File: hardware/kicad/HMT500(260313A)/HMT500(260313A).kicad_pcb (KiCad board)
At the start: 6 copper layers, 56.5 x 23 mm, 110 parts, among them J1 SM08B-GHS-TB, J2 TC2030-IDC-NL, J3 SM04B-SRSS-TB, J5 CHASSIS wire, U1 TPS26600PWPR, U10 TPS26611DDFR, U11 THVD2410DGKR, U12 OPA197IDBVR, U13 OPA197IDBVR, U14 SN74LVC2G32DCUR, U15 LMR51606YFDBVR, U2 LMR51606YFDBVR, U3 TPS7A2033PDBVR, U4 STM32G0B1CCT6, U5 PCAP04-AQFM-24, U6 ADS1220IPWR, U7 DAC8760IPWP, U8 DAC8760IPWP, U9 TPS26611DDFR

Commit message: HMT500 A5 배선 연결 완료 및 제조 검토 패키지 생성
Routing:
- net SWCLK: track 7.07 -> 41.5 mm, vias 0 -> 4
- net RS485_A_EXT: track 2.83 -> 30.3 mm, vias 0 -> 4
- net VIN_P: track 49.8 -> 69.3 mm, vias 6 -> 8
- net OUT1_SGOOD: track 0.82 -> 19.3 mm, vias 0 -> 2
- net DAC_MOSI: track 55.5 -> 44.6 mm, vias 6 -> 5
- net EF_RTN: track 60.4 -> 50.3 mm, vias 8 -> 6
- net VAO: track 95.8 -> 91.0 mm
- net DAC2_LATCH: track 44.5 -> 48.3 mm, vias 5 -> 6
- net +3V3: track 166.7 -> 163.9 mm
- net CDC_SCK: track 17.2 -> 14.5 mm
- net CDC_MOSI: track 9.56 -> 6.89 mm
- net VIN_SENSE: track 13.3 -> 11.0 mm
- net PT_P: track 15.0 -> 13.6 mm
- net SWDIO: track 43.0 -> 41.9 mm
- net DAC2_SCLK: track 34.7 -> 33.7 mm
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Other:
- board text added: "HMT500 A5"
- board text removed: "HMT500 A4"

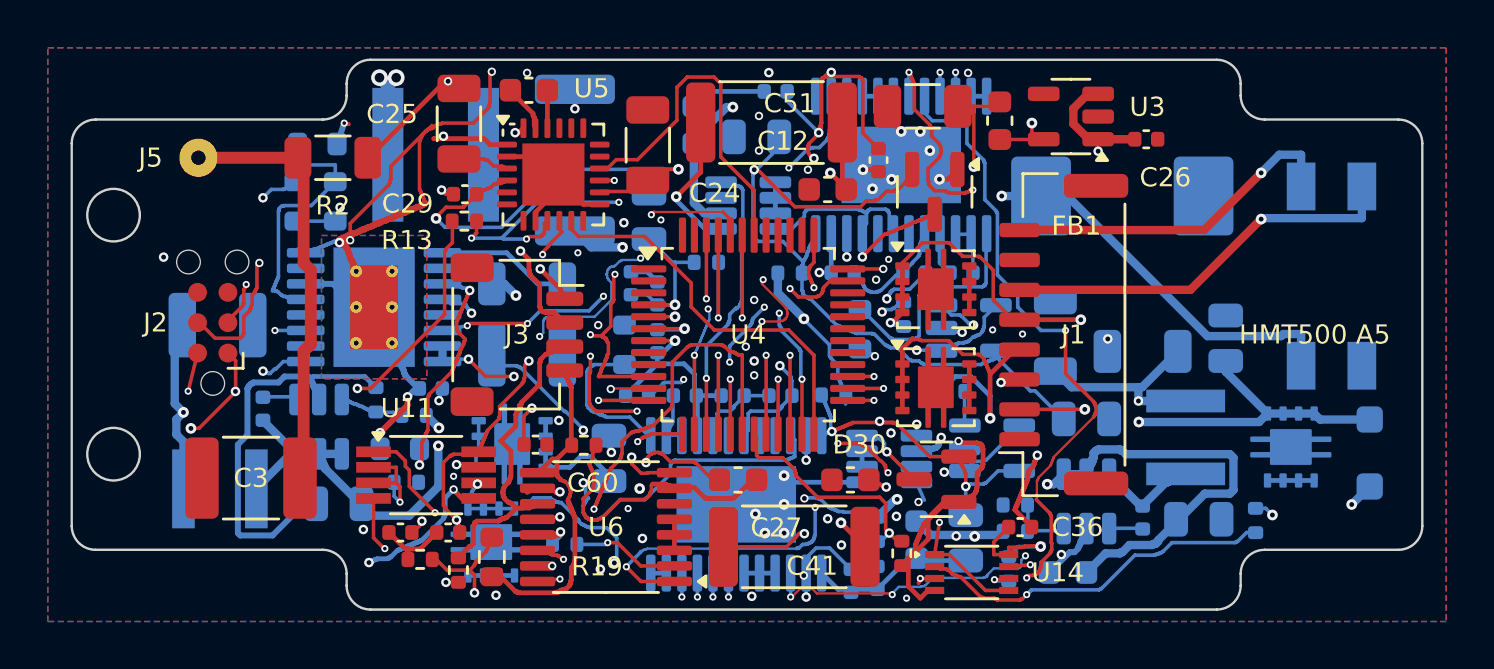
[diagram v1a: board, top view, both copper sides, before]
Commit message: HMT500 A5-R1 실제 실크 근접 배치 및 거버 재생성
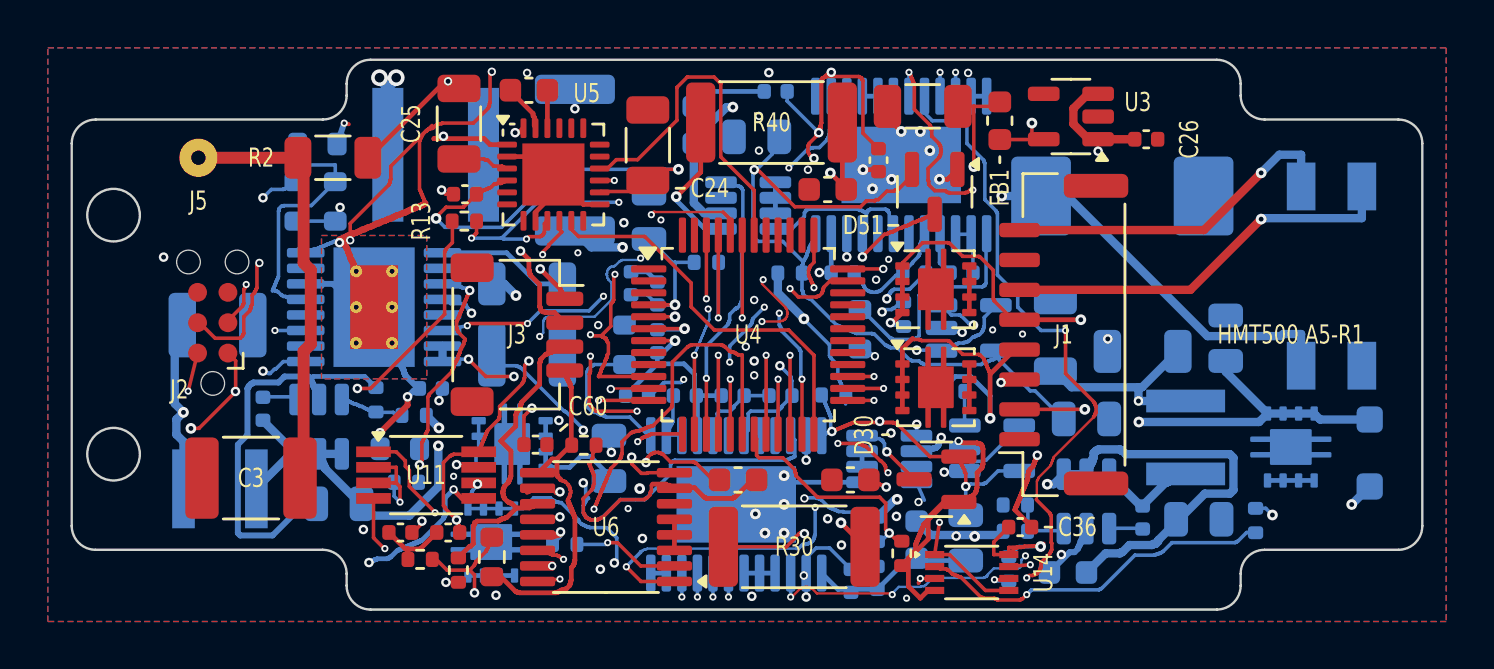
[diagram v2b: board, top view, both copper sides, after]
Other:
- board text added: "HMT500 A5-R1"
- board text removed: "HMT500 A5"

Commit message: Match HMT500 BOM to LCSC catalog and correct procurement specifications
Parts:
- C22: value 330p C0G 1% -> 330p C0G 2%
- R19: value 4.02k 0.02% 5ppm -> 4.02k 0.1% 25ppm

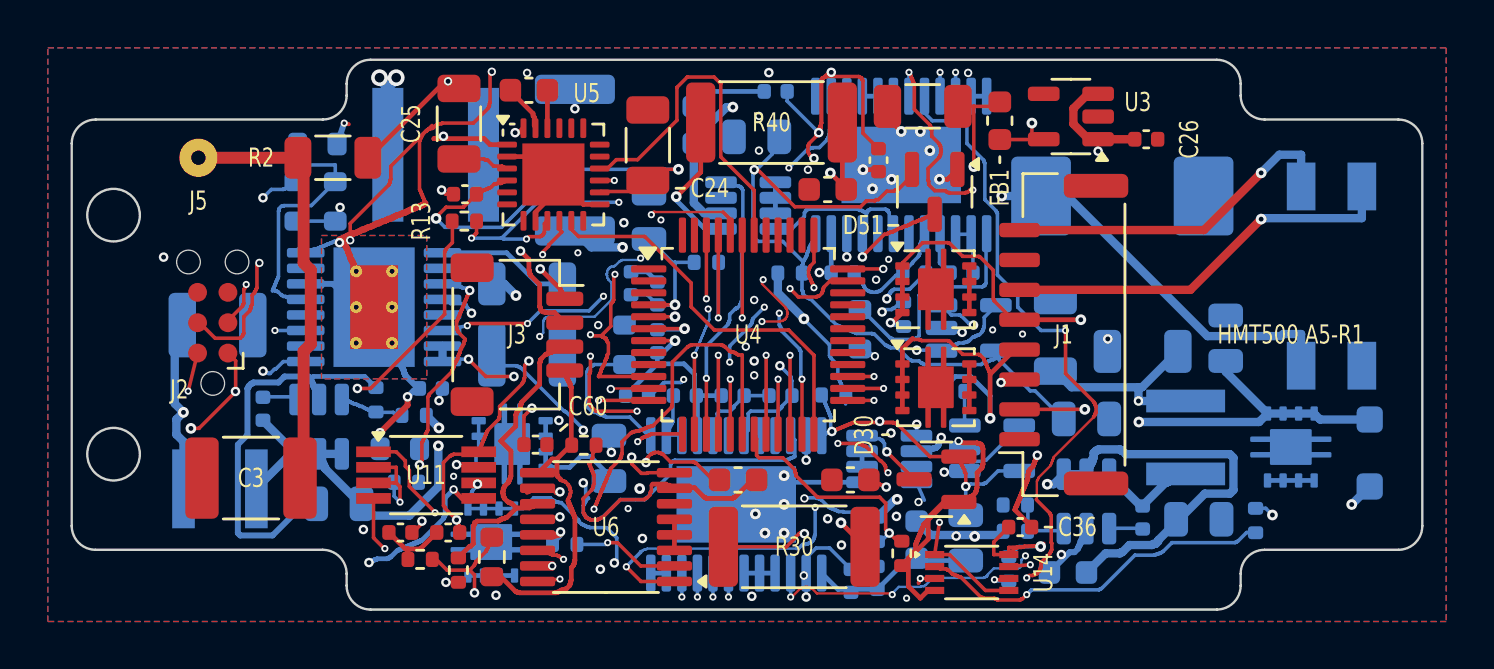
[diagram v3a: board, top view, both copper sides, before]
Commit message: Place HMT500 references beside components and add top DOTECH wordmark
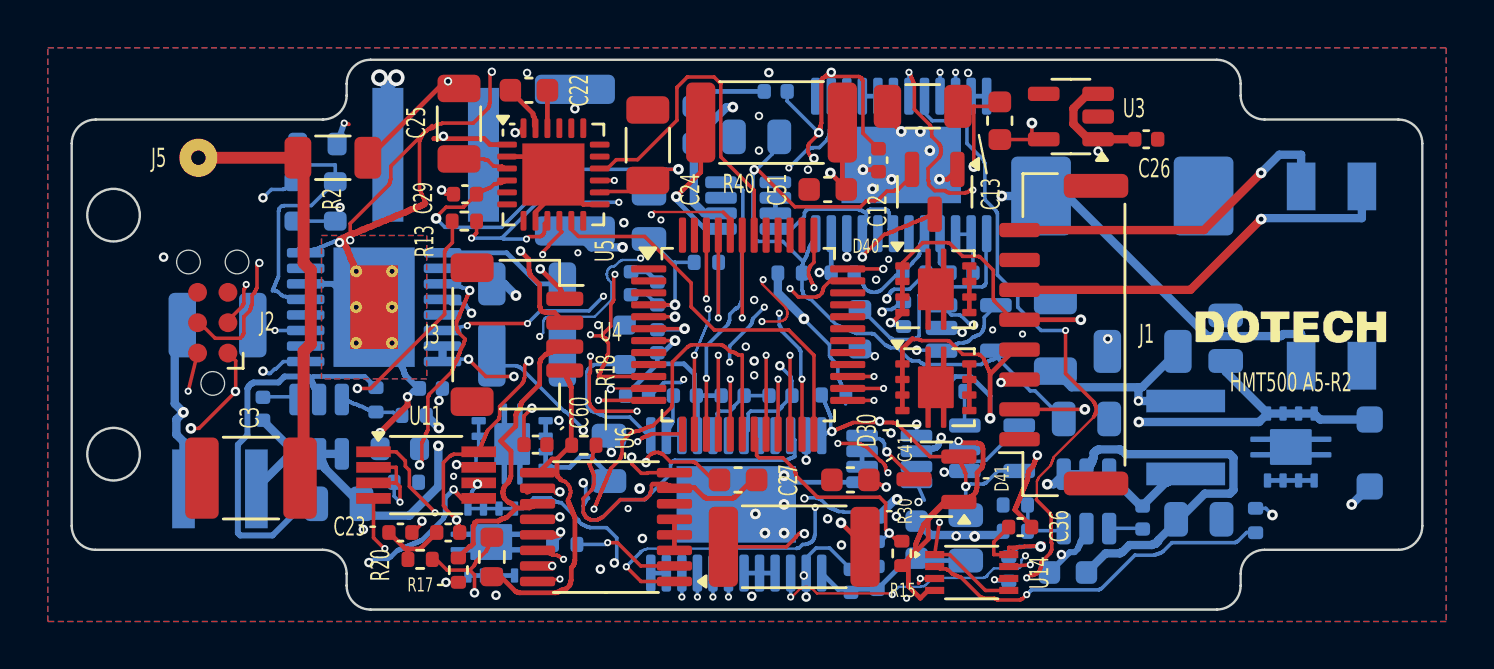
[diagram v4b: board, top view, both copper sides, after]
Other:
- board text added: "HMT500 A5-R2"
- board text removed: "HMT500 A5-R1"
